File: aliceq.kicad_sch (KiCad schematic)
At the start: 139 parts, among them J1 ISP-6, SW1 SW_Push, U1 ATmega32U4-AU, U2 PRTR5V0U2X, Y1 CLK

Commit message: Antes del ruteo y posicionamiento de partes
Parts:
- removed MX16: MX-NoLED, MX_Only:MXOnly-1U-NoLED, symbol forty-rescue:MX-NoLED-MX_Alps_Hybrid
- added D54, D55, D56, D57, D58, D59, D60, D61, D62, D63, D64, D65, D66, D67: D_Small, Diode_SMD:D_SOD-123, symbol Device:D_Small
- added MX1: MX-NoLED, MX_Only:MXOnly-2U-NoLED, symbol forty-rescue:MX-NoLED-MX_Alps_Hybrid
- added MX54, MX55, MX56, MX57, MX58, MX59, MX60, MX62, MX65, MX69: MX-NoLED, MX_Only:MXOnly-1U-NoLED, symbol forty-rescue:MX-NoLED-MX_Alps_Hybrid
- added MX61: MX-NoLED, MX_Only:MXOnly-1.75U-NoLED, symbol forty-rescue:MX-NoLED-MX_Alps_Hybrid
- added MX63, MX73: MX-NoLED, MX_Only:MXOnly-1.25U-NoLED, symbol forty-rescue:MX-NoLED-MX_Alps_Hybrid
- added MX64, MX66, MX71, MX72: MX-NoLED, MX_Only:MXOnly-1.5U-NoLED, symbol forty-rescue:MX-NoLED-MX_Alps_Hybrid
- added MX67: MX-NoLED, MX_Only:MXOnly-2.25U-ReversedStabilizers-NoLED, symbol forty-rescue:MX-NoLED-MX_Alps_Hybrid
- added MX68: MX-NoLED, MX_Only:MXOnly-2U-ReversedStabilizers-NoLED, symbol forty-rescue:MX-NoLED-MX_Alps_Hybrid
- added MX70: MX-NoLED, MX_Only:MXOnly-2.75U-ReversedStabilizers-NoLED, symbol forty-rescue:MX-NoLED-MX_Alps_Hybrid
- MX17, MX42: footprint MX_Only:MXOnly-1.25U-NoLED -> MX_Only:MXOnly-1U-NoLED
- MX18: footprint MX_Only:MXOnly-1U-NoLED -> MX_Only:MXOnly-1.5U-NoLED
- MX29: footprint MX_Only:MXOnly-1.75U-NoLED -> MX_Only:MXOnly-1U-NoLED
- MX31: footprint MX_Only:MXOnly-1.75U-NoLED -> MX_Only:MXOnly-1.5U-NoLED
- MX45: footprint MX_Only:MXOnly-1U-NoLED -> MX_Only:MXOnly-2.25U-ReversedStabilizers-NoLED
- MX46: footprint MX_Only:MXOnly-1.25U-NoLED -> MX_Only:MXOnly-1.75U-NoLED
- MX47: footprint MX_Only:MXOnly-2U-NoLED -> MX_Only:MXOnly-2.75U-NoLED
- MX48: footprint MX_Only:MXOnly-1U-NoLED -> MX_Only:MXOnly-2.25U-NoLED
- MX49: footprint MX_Only:MXOnly-2.75U-NoLED -> MX_Only:MXOnly-1U-NoLED
- renumbered D54 to D68, D55 to D69, D56 to D70, D57 to D71, D58 to D72, D59 to D73, D60 to D74, D61 to D75, D62 to D76, D63 to D77, D64 to D78, D65 to D79, MX9 to MX10, MX10 to MX11, MX11 to MX12, MX12 to MX13, MX13 to MX14, MX14 to MX15, MX15 to MX16, MX1 to MX2, MX2 to MX3, MX3 to MX4, MX4 to MX5, MX5 to MX6, MX6 to MX7, MX7 to MX8, MX8 to MX9
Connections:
- net COL0: now also MX17.1 (COL), MX32.1 (COL), MX49.1 (COL); no longer MX30.1 (COL)
- net COL1: now also MX18.1 (COL), MX33.1 (COL), MX46.1 (COL), MX48.1 (COL), MX63.1 (COL), MX64.1 (COL); no longer MX17.1 (COL), MX31.1 (COL), MX45.1 (COL)
- net COL10: now also MX27.1 (COL), MX42.1 (COL), MX58.1 (COL), MX71.1 (COL); no longer MX26.1 (COL), MX40.1 (COL), MX50.1 (COL)
- net COL11: now also MX28.1 (COL), MX43.1 (COL), MX59.1 (COL); no longer MX27.1 (COL), MX41.1 (COL)
- net COL12: now also MX29.1 (COL), MX44.1 (COL), MX60.1 (COL); no longer MX28.1 (COL), MX42.1 (COL), MX51.1 (COL)
- net COL13: now also MX30.1 (COL), MX47.1 (COL), MX1.1 (COL), MX61.1 (COL); no longer MX43.1 (COL), MX52.1 (COL)
- net COL14: now also MX31.1 (COL), MX45.1 (COL), MX62.1 (COL), MX72.1 (COL); no longer MX29.1 (COL), MX44.1 (COL), MX53.1 (COL)
- net COL2: now also MX19.1 (COL), MX34.1 (COL), MX50.1 (COL), MX65.1 (COL); no longer MX18.1 (COL), MX32.1 (COL)
- net COL3: now also MX20.1 (COL), MX35.1 (COL), MX51.1 (COL), MX66.1 (COL); no longer MX19.1 (COL), MX33.1 (COL), MX46.1 (COL)
- net COL4: now also MX21.1 (COL), MX36.1 (COL), MX52.1 (COL); no longer MX20.1 (COL), MX34.1 (COL)
- net COL5: now also MX22.1 (COL), MX37.1 (COL), MX53.1 (COL), MX67.1 (COL), MX68.1 (COL); no longer MX21.1 (COL), MX35.1 (COL), MX47.1 (COL)
- net COL6: now also MX23.1 (COL), MX38.1 (COL), MX54.1 (COL), MX69.1 (COL), MX73.1 (COL); no longer MX22.1 (COL), MX36.1 (COL), MX48.1 (COL)
- net COL7: now also MX24.1 (COL), MX39.1 (COL), MX55.1 (COL), MX70.1 (COL); no longer MX23.1 (COL), MX37.1 (COL)
- net COL8: now also MX25.1 (COL), MX40.1 (COL), MX56.1 (COL); no longer MX24.1 (COL), MX38.1 (COL), MX49.1 (COL)
- net COL9: now also MX26.1 (COL), MX41.1 (COL), MX57.1 (COL); no longer MX25.1 (COL), MX39.1 (COL)
- net ROW1: now also D30.1 (K)
- net ROW2: no longer D30.1 (K)
- net ROW3: now also D54.1 (K), D55.1 (K), D56.1 (K), D57.1 (K), D58.1 (K), D59.1 (K)
- net at MX44.2 (ROW): now also D43.2 (A); no longer D44.2 (A)
- net at MX53.2 (ROW): now also D50.2 (A); no longer D53.2 (A)
- net at D29.2 (A): now also MX30.2 (ROW); no longer MX29.2 (ROW)
- net at D14.2 (A), MX15.2 (ROW): now also MX1.2 (ROW)
- net at MX23.2 (ROW): now also D22.2 (A); no longer D23.2 (A)
- net at MX22.2 (ROW): now also D21.2 (A); no longer D22.2 (A)
- net at MX21.2 (ROW): now also D20.2 (A); no longer D21.2 (A)
- net at MX20.2 (ROW): now also D19.2 (A); no longer D20.2 (A)
- net at MX19.2 (ROW): now also D18.2 (A); no longer D19.2 (A)
- net at MX18.2 (ROW): now also D17.2 (A); no longer D18.2 (A)
- net at MX17.2 (ROW): now also D16.2 (A); no longer D17.2 (A)
- net at D24.2 (A): now also MX25.2 (ROW); no longer MX24.2 (ROW)
- net at D25.2 (A): now also MX26.2 (ROW); no longer MX25.2 (ROW)
- net at D26.2 (A): now also MX27.2 (ROW); no longer MX26.2 (ROW)
- net at D27.2 (A): now also MX28.2 (ROW); no longer MX27.2 (ROW)
- net at D28.2 (A): now also MX29.2 (ROW); no longer MX28.2 (ROW)
- net at MX37.2 (ROW): now also D36.2 (A); no longer D37.2 (A)
- net at MX36.2 (ROW): now also D35.2 (A); no longer D36.2 (A)
- net at MX35.2 (ROW): now also D34.2 (A); no longer D35.2 (A)
- net at MX34.2 (ROW): now also D33.2 (A); no longer D34.2 (A)
- net at MX33.2 (ROW): now also D32.2 (A), MX46.2 (ROW); no longer D33.2 (A)
- net at MX32.2 (ROW): now also D31.2 (A); no longer D32.2 (A)
- net at MX31.2 (ROW): now also D30.2 (A); no longer D31.2 (A)
- net at MX38.2 (ROW): now also D37.2 (A); no longer D38.2 (A)
- net at D39.2 (A): now also MX40.2 (ROW); no longer MX39.2 (ROW)
- net at D40.2 (A): now also MX41.2 (ROW); no longer MX40.2 (ROW)
- net at D41.2 (A): now also MX42.2 (ROW); no longer MX41.2 (ROW)
- net at D42.2 (A): now also MX43.2 (ROW); no longer MX42.2 (ROW)
- net at MX48.2 (ROW): now also D46.2 (A), MX63.2 (ROW); no longer D48.2 (A)
- net at D47.2 (A): now also MX50.2 (ROW); no longer MX47.2 (ROW)
- net at D45.2 (A): now also MX49.2 (ROW); no longer MX45.2 (ROW)
- net at D49.2 (A): now also MX52.2 (ROW); no longer MX49.2 (ROW)
- net at D51.2 (A): now also MX54.2 (ROW); no longer MX51.2 (ROW)
- net at D52.2 (A): now also MX55.2 (ROW); no longer MX52.2 (ROW)
- new net: D64.2 (A), MX69.2 (ROW), MX73.2 (ROW)
- new net: D57.2 (A), MX60.2 (ROW)
- new net: D67.2 (A), MX72.2 (ROW)
- new net: D65.2 (A), MX70.2 (ROW)
- new net: D56.2 (A), MX59.2 (ROW)
- new net: D61.2 (A), MX65.2 (ROW)
- new net: D62.2 (A), MX66.2 (ROW)
- new net: D66.2 (A), MX71.2 (ROW)
- new net: D55.2 (A), MX58.2 (ROW)
- new net: D60.2 (A), MX64.2 (ROW)
- new net: D58.2 (A), MX47.2 (ROW), MX61.2 (ROW)
- new net: D44.2 (A), MX45.2 (ROW)
- new net: D48.2 (A), MX51.2 (ROW)
- new net: D53.2 (A), MX56.2 (ROW)
- new net: D59.2 (A), MX62.2 (ROW)
- new net: D63.2 (A), MX67.2 (ROW), MX68.2 (ROW)
- new net: D54.2 (A), MX57.2 (ROW)
- new net: D38.2 (A), MX39.2 (ROW)
- new net: D23.2 (A), MX24.2 (ROW)
- new net ROW4: D60.1 (K), D61.1 (K), D62.1 (K), D63.1 (K), D64.1 (K), D65.1 (K), D66.1 (K), D67.1 (K)
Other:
- moved on the sheet: D68, D69, D70, D71, D72, D73, D74, D75, D76, D77, D78, D79

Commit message: progreso del fin de semana
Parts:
- added D80, D81, D82: LED_Small, LED_THT:LED_D1.8mm_W3.3mm_H2.4mm, symbol Device:LED_Small
- C1, C2, C3, C4, C5, C6: footprint Capacitor_SMD:C_0805_2012Metric_Pad1.15x1.40mm_HandSolder -> Capacitor_SMD:C_0603_1608Metric
- R1, R2, R3, R4, R5, R6: footprint Resistor_SMD:R_0805_2012Metric_Pad1.15x1.40mm_HandSolder -> Resistor_SMD:R_0603_1608Metric
- U1: value ATmega32U4-AU -> ATmega32U4-MU; footprint Package_QFP:TQFP-44_10x10mm_P0.8mm -> Package_DFN_QFN:QFN-44-1EP_7x7mm_P0.5mm_EP5.15x5.15mm
- USB1: footprint Type-C:HRO-TYPE-C-31-M-12-HandSoldering -> Type-C:HRO-TYPE-C-31-M-12-Assembly
- Y1: footprint Crystal:Crystal_SMD_3225-4Pin_3.2x2.5mm_HandSoldering -> Crystal:Crystal_SMD_3225-4Pin_3.2x2.5mm
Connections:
- net ROW1: now also U1.41 (PF0); no longer U1.30 (PB6)
- net ROW4: now also U1.30 (PB6)
- net DN: now reaches R2.1, U2.3 (IO2), USB1.5 (DN2), USB1.7 (DN1)
- net DP: now reaches R3.2, U2.2 (IO1), USB1.6 (DP1), USB1.8 (DP2)
- no-connect marks 6 -> 5

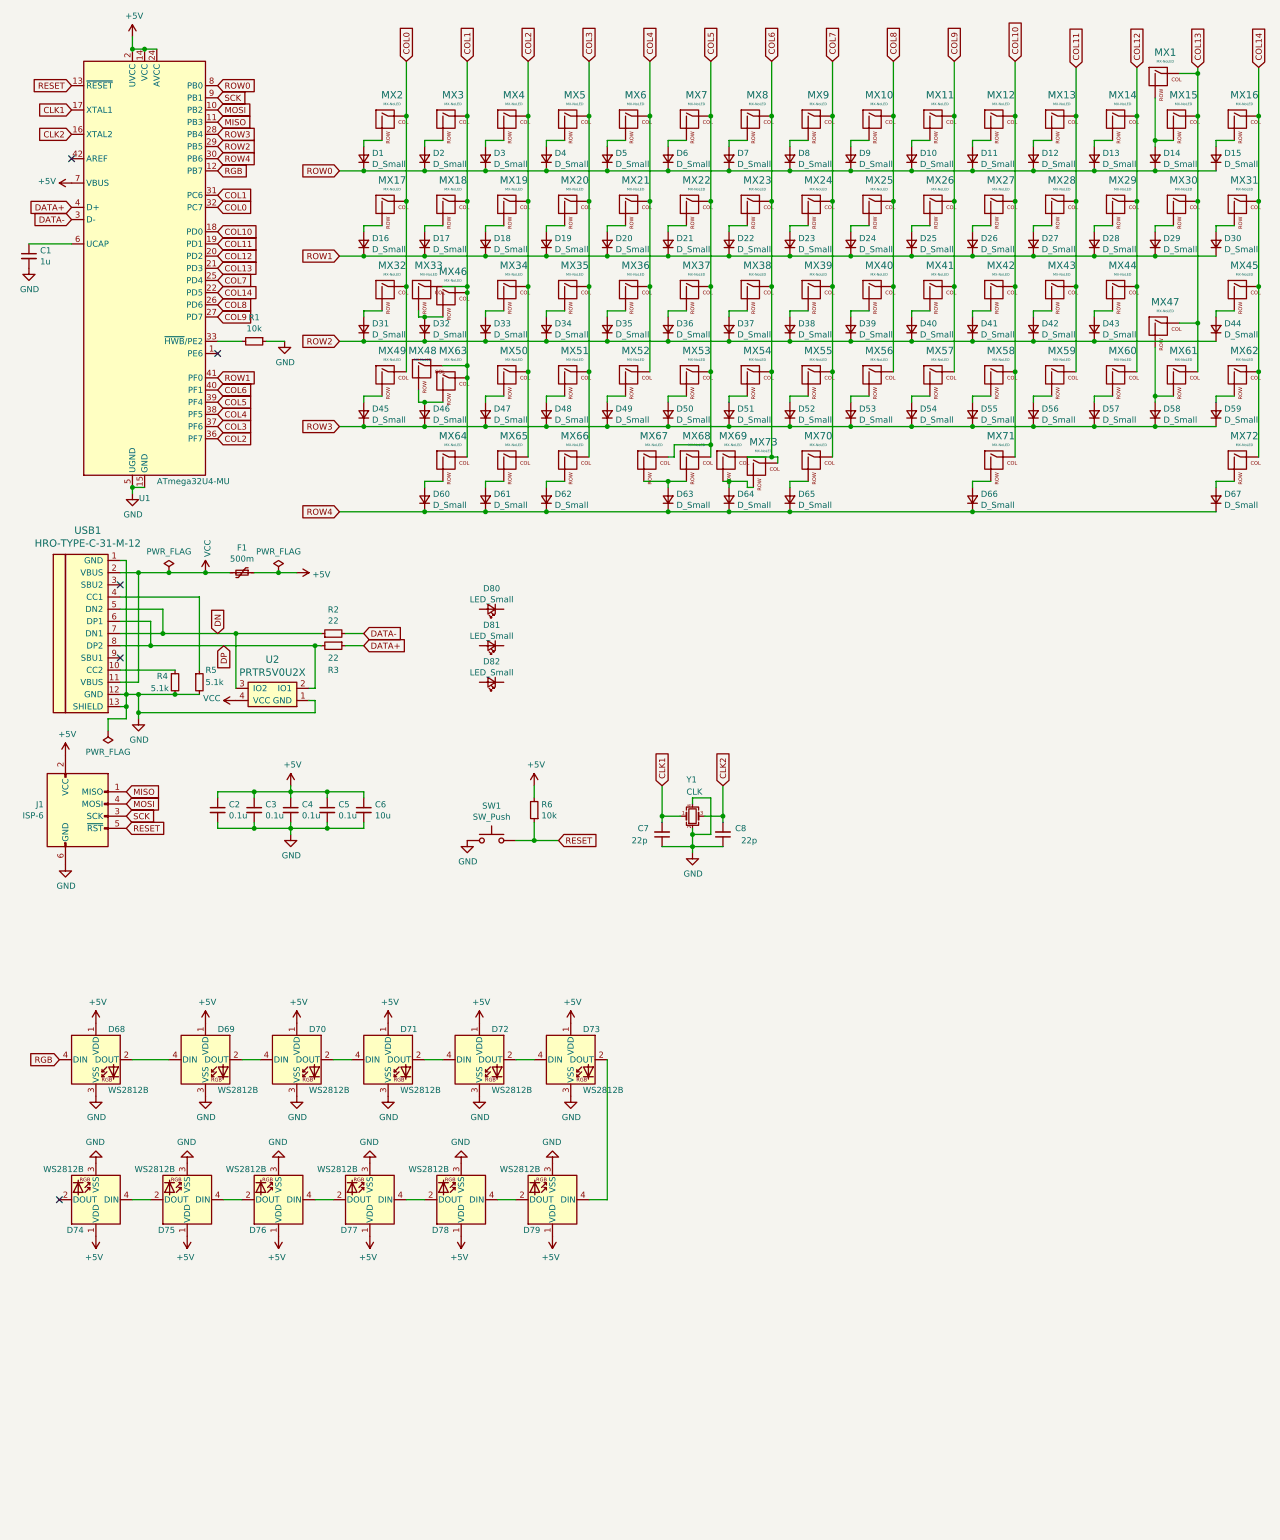
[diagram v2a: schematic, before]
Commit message: Terminado el ruteado, faltan los leds y el RGB
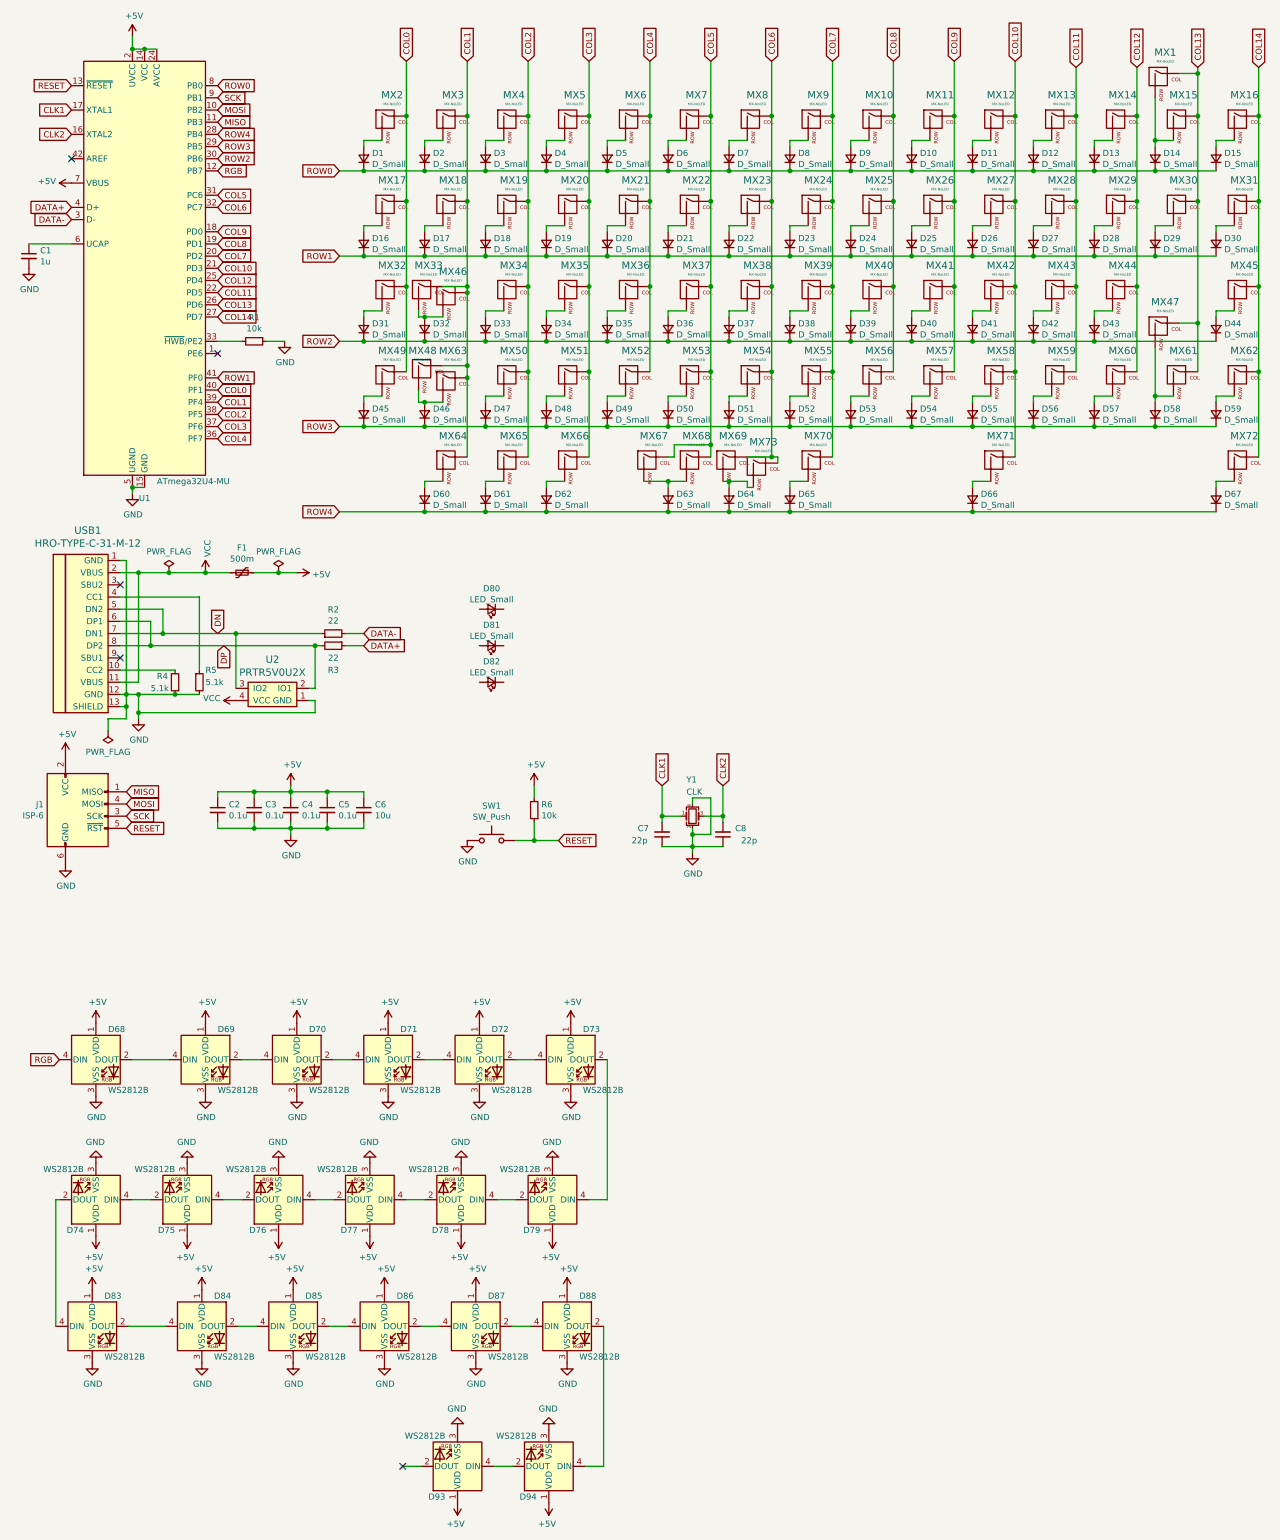
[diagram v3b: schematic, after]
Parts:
- added D83, D84, D85, D86, D87, D88, D93, D94: WS2812B, LED_SMD:LED_WS2812B_PLCC4_5.0x5.0mm_P3.2mm, symbol LED:WS2812B
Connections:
- net +5V: now also D83.1 (VDD), D84.1 (VDD), D85.1 (VDD), D86.1 (VDD), D87.1 (VDD), D88.1 (VDD), D93.1 (VDD), D94.1 (VDD)
- net COL0: now also U1.40 (PF1); no longer U1.32 (PC7)
- net COL1: now also U1.39 (PF4); no longer U1.31 (PC6)
- net COL10: now also U1.21 (PD3); no longer U1.18 (PD0)
- net COL11: now also U1.22 (PD5); no longer U1.19 (PD1)
- net COL12: now also U1.25 (PD4); no longer U1.20 (PD2)
- net COL13: now also U1.26 (PD6); no longer U1.21 (PD3)
- net COL14: now also U1.27 (PD7); no longer U1.22 (PD5)
- net COL2: now also U1.38 (PF5); no longer U1.36 (PF7)
- net COL4: now also U1.36 (PF7); no longer U1.38 (PF5)
- net COL5: now also U1.31 (PC6); no longer U1.39 (PF4)
- net COL6: now also U1.32 (PC7); no longer U1.40 (PF1)
- net COL7: now also U1.20 (PD2); no longer U1.25 (PD4)
- net COL8: now also U1.19 (PD1); no longer U1.26 (PD6)
- net COL9: now also U1.18 (PD0); no longer U1.27 (PD7)
- net GND: now also D83.3 (VSS), D84.3 (VSS), D85.3 (VSS), D86.3 (VSS), D87.3 (VSS), D88.3 (VSS), D93.3 (VSS), D94.3 (VSS)
- net ROW2: now also U1.30 (PB6); no longer U1.29 (PB5)
- net ROW3: now also U1.29 (PB5); no longer U1.28 (PB4)
- net ROW4: now also U1.28 (PB4); no longer U1.30 (PB6)
- net at D74.2 (DOUT): now also D83.4 (DIN)
- new net: D86.2 (DOUT), D87.4 (DIN)
- new net: D85.2 (DOUT), D86.4 (DIN)
- new net: D87.2 (DOUT), D88.4 (DIN)
- new net: D83.2 (DOUT), D84.4 (DIN)
- new net: D84.2 (DOUT), D85.4 (DIN)
- new net: D88.2 (DOUT), D94.4 (DIN)
- new net: D93.4 (DIN), D94.2 (DOUT)

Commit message: Probando arte
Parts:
- C7, C8: footprint Capacitor_SMD:C_0805_2012Metric_Pad1.15x1.40mm_HandSolder -> Capacitor_SMD:C_0603_1608Metric
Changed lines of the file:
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@@
       (effects (font (size 1.27 1.27)) (justify right))
     )
-    (property "Footprint" "Capacitor_SMD:C_0805_2012Metric_Pad1.15x1.40mm_HandSolder" (id 2) (at 148.59 185.42 0)
+    (property "Footprint" "Capacitor_SMD:C_0603_1608Metric" (id 2) (at 148.59 185.42 0)
       (effects (font (size 1.27 1.27)) hide)
     )
@@
       (effects (font (size 1.27 1.27)) (justify right))
     )
-    (property "Footprint" "Capacitor_SMD:C_0805_2012Metric_Pad1.15x1.40mm_HandSolder" (id 2) (at 161.29 185.42 0)
+    (property "Footprint" "Capacitor_SMD:C_0603_1608Metric" (id 2) (at 161.29 185.42 0)
       (effects (font (size 1.27 1.27)) hide)
     )
@@
     )
     (path "/00000000-0000-0000-0000-00005fe7b819"
-      (reference "C7") (unit 1) (value "22p") (footprint "Capacitor_SMD:C_0805_2012Metric_Pad1.15x1.40mm_HandSolder")
+      (reference "C7") (unit 1) (value "22p") (footprint "Capacitor_SMD:C_0603_1608Metric")
     )
     (path "/00000000-0000-0000-0000-00005fe7dfa3"
-      (reference "C8") (unit 1) (value "22p") (footprint "Capacitor_SMD:C_0805_2012Metric_Pad1.15x1.40mm_HandSolder")
+      (reference "C8") (unit 1) (value "22p") (footprint "Capacitor_SMD:C_0603_1608Metric")
     )
     (path "/00000000-0000-0000-0000-00005ff0bb5b"

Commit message: hotswap done
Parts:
- removed D15, D61: D_Small, Diode_SMD:D_SOD-123, symbol Device:D_Small
- removed MX15, MX16, MX33, MX65, MX69: MX-NoLED, MX_Only:MXOnly-1U-NoLED, symbol forty-rescue:MX-NoLED-MX_Alps_Hybrid
- removed MX47: MX-NoLED, MX_Only:MXOnly-2.75U-NoLED, symbol forty-rescue:MX-NoLED-MX_Alps_Hybrid
- removed MX63: MX-NoLED, MX_Only:MXOnly-1.25U-NoLED, symbol forty-rescue:MX-NoLED-MX_Alps_Hybrid
- removed MX67: MX-NoLED, MX_Only:MXOnly-2.25U-ReversedStabilizers-NoLED, symbol forty-rescue:MX-NoLED-MX_Alps_Hybrid
- MX1: footprint MX_Only:MXOnly-2U-NoLED -> MX_Only:MXOnly-2U-Hotswap
- MX10, MX11, MX12, MX13, MX14, MX17, MX19, MX2, MX20, MX21, MX22, MX23, MX24, MX25, MX26, MX27, MX28, MX29, MX3, MX30, MX32, MX34, MX35, MX36, MX37, MX38, MX39, MX4, MX40, MX41, MX42, MX43, MX44, MX49, MX5, MX50, MX51, MX52, MX53, MX54, MX55, MX56, MX57, MX58, MX59, MX6, MX60, MX62, MX7, MX8, MX9: footprint MX_Only:MXOnly-1U-NoLED -> MX_Only:MXOnly-1U-Hotswap
- MX18, MX31, MX64, MX66, MX71, MX72: footprint MX_Only:MXOnly-1.5U-NoLED -> MX_Only:MXOnly-1.5U-Hotswap
- MX45: footprint MX_Only:MXOnly-2.25U-ReversedStabilizers-NoLED -> MX_Only:MXOnly-2.25U-Hotswap-ReversedStabilizers
- MX46, MX61: footprint MX_Only:MXOnly-1.75U-NoLED -> MX_Only:MXOnly-1.75U-Hotswap
- MX48: footprint MX_Only:MXOnly-2.25U-NoLED -> MX_Only:MXOnly-2.25U-Hotswap
- MX68: footprint MX_Only:MXOnly-2U-ReversedStabilizers-NoLED -> MX_Only:MXOnly-2U-Hotswap-ReversedStabilizers
- MX70: footprint MX_Only:MXOnly-2.75U-ReversedStabilizers-NoLED -> MX_Only:MXOnly-2.75U-Hotswap-ReversedStabilizers
- MX73: footprint MX_Only:MXOnly-1.25U-NoLED -> MX_Only:MXOnly-1.25U-Hotswap
